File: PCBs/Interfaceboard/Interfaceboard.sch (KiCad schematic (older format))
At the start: 0 parts

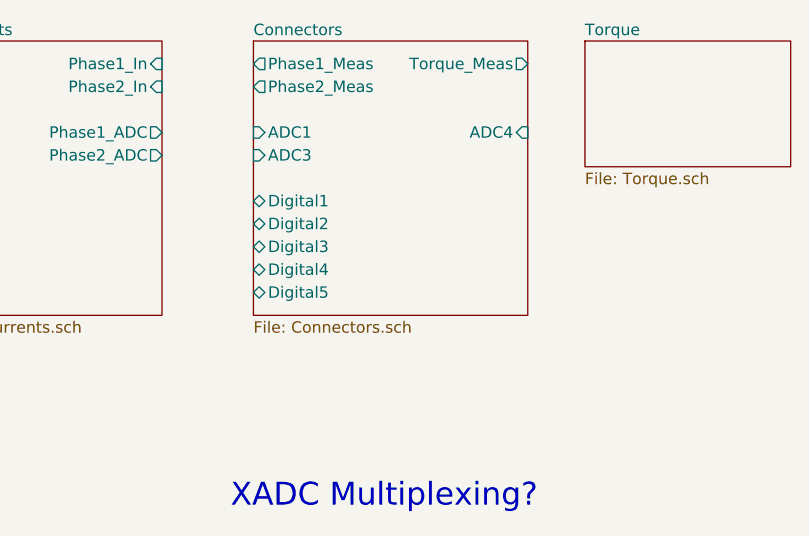
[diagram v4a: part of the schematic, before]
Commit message: Finished schematics for analog interface board. Ready for review and then PCB design.
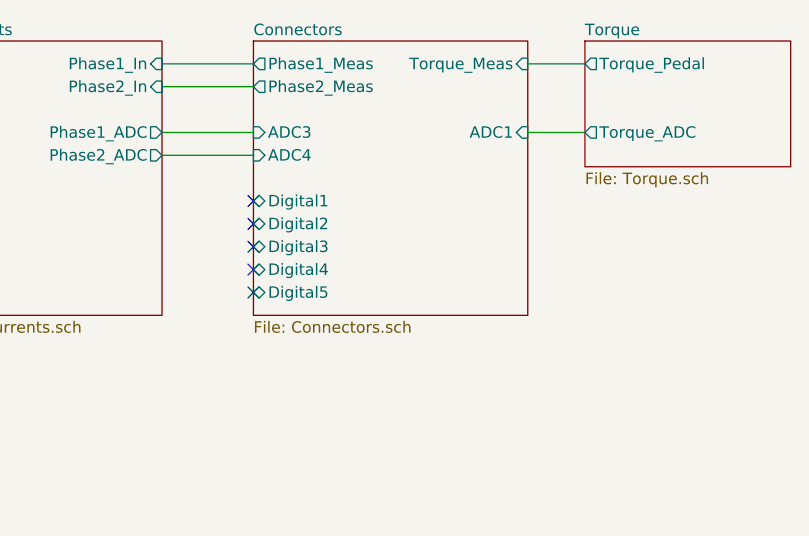
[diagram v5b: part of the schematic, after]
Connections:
- no-connect marks 0 -> 5
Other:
- note removed: "XADC Multiplexing?"
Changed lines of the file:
@@
 $EndDescr
-$Sheet
-S 4900 2400 1200 1200
-U 6040B42D
-F0 "Connectors" 50
-F1 "Connectors.sch" 50
-F2 "Phase1_Meas" O L 4900 2500 50
-F3 "Phase2_Meas" O L 4900 2600 50
-F4 "Torque_Meas" O R 6100 2500 50
-F5 "ADC1" I L 4900 2800 50
-F6 "ADC3" I L 4900 2900 50
-F7 "ADC4" I R 6100 2800 50
-F8 "Digital1" B L 4900 3100 50
-F9 "Digital2" B L 4900 3200 50
-F10 "Digital3" B L 4900 3300 50
-F11 "Digital4" B L 4900 3400 50
-F12 "Digital5" B L 4900 3500 50
-$EndSheet
 $Sheet
 S 3550 2400 950  1200
@@
 F0 "Torque" 50
 F1 "Torque.sch" 50
+F2 "Torque_Pedal" O L 6350 2500 50
+F3 "Torque_ADC" O L 6350 2800 50
 $EndSheet
-Text Notes 4800 4450 0    100  ~ 0
-XADC Multiplexing?
+Wire Wire Line
+	6350 2500 6100 2500
+Wire Wire Line
+	6100 2800 6350 2800
+Wire Wire Line
+	4500 2500 4900 2500
+Wire Wire Line
+	4900 2600 4500 2600
+Wire Wire Line
+	4500 2800 4900 2800
+Wire Wire Line
+	4900 2900 4500 2900
+$Sheet
+S 4900 2400 1200 1200
+U 6040B42D
+F0 "Connectors" 50
+F1 "Connectors.sch" 50
+F2 "Phase1_Meas" O L 4900 2500 50
+F3 "Phase2_Meas" O L 4900 2600 50
+F4 "Torque_Meas" I R 6100 2500 50
+F5 "ADC3" I L 4900 2800 50
+F6 "ADC4" I L 4900 2900 50
+F7 "ADC1" I R 6100 2800 50
+F8 "Digital1" B L 4900 3100 50
+F9 "Digital2" B L 4900 3200 50
+F10 "Digital3" B L 4900 3300 50
+F11 "Digital4" B L 4900 3400 50
+F12 "Digital5" B L 4900 3500 50
+$EndSheet
+NoConn ~ 4900 3100
+NoConn ~ 4900 3200
+NoConn ~ 4900 3300
+NoConn ~ 4900 3400
+NoConn ~ 4900 3500
 $EndSCHEMATC

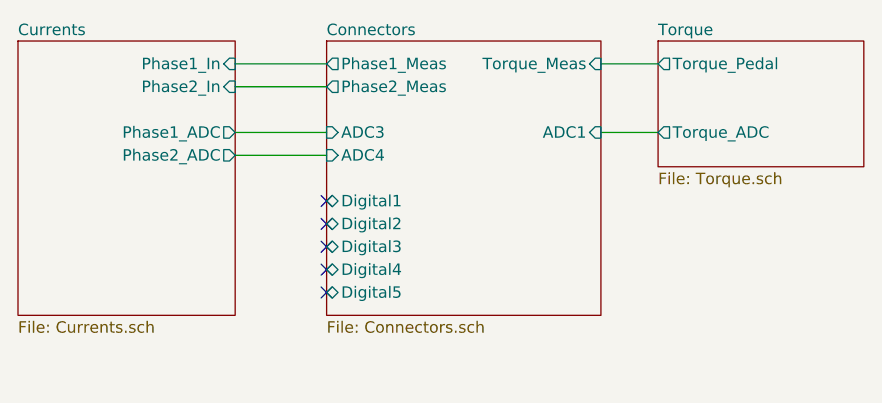
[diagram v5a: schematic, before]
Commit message: Added test points and final associated footprints. Made outline for PCB.
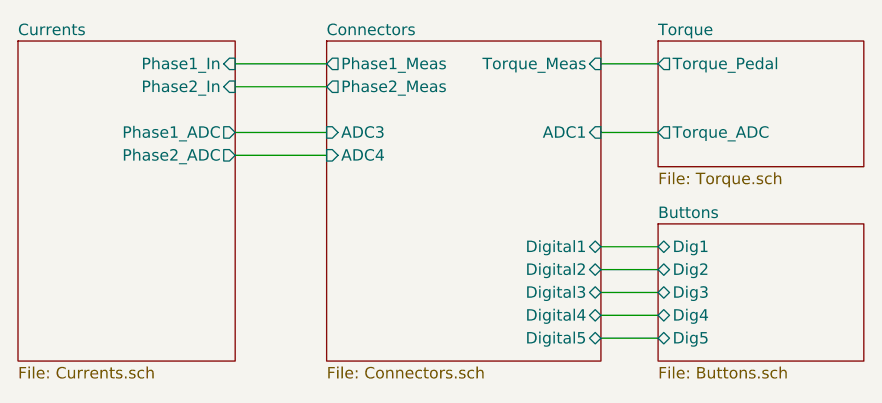
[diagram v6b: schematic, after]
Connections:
- no-connect marks 5 -> 0
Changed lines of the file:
@@
 $Descr A4 11693 8268
 encoding utf-8
-Sheet 1 4
-Title "Interface Board for Control of PMAC Motor in Electric Go-Kart"
-Date "2021-03-04"
+Sheet 1 5
+Title "Analog Board for Control of PMAC Motor in Electric Go-Kart"
+Date "2021-03-13"
 Rev "Version 1"
 Comp "University of Southern Denmark"
@@
 $EndDescr
 $Sheet
-S 3550 2400 950  1200
+S 3550 2400 950  1400
 U 6040B450
 F0 "Currents" 50
@@
 	4900 2900 4500 2900
 $Sheet
-S 4900 2400 1200 1200
+S 4900 2400 1200 1400
 U 6040B42D
 F0 "Connectors" 50
@@
 F6 "ADC4" I L 4900 2900 50
 F7 "ADC1" I R 6100 2800 50
-F8 "Digital1" B L 4900 3100 50
-F9 "Digital2" B L 4900 3200 50
-F10 "Digital3" B L 4900 3300 50
-F11 "Digital4" B L 4900 3400 50
-F12 "Digital5" B L 4900 3500 50
+F8 "Digital1" B R 6100 3300 50
+F9 "Digital2" B R 6100 3400 50
+F10 "Digital3" B R 6100 3500 50
+F11 "Digital4" B R 6100 3600 50
+F12 "Digital5" B R 6100 3700 50
 $EndSheet
-NoConn ~ 4900 3100
-NoConn ~ 4900 3200
-NoConn ~ 4900 3300
-NoConn ~ 4900 3400
-NoConn ~ 4900 3500
+$Sheet
+S 6350 3200 900  600
+U 604F3ED7
+F0 "Buttons" 50
+F1 "Buttons.sch" 50
+F2 "Dig1" B L 6350 3300 50
+F3 "Dig2" B L 6350 3400 50
+F4 "Dig3" B L 6350 3500 50
+F5 "Dig4" B L 6350 3600 50
+F6 "Dig5" B L 6350 3700 50
+$EndSheet
+Wire Wire Line
+	6350 3300 6100 3300
+Wire Wire Line
+	6100 3400 6350 3400
+Wire Wire Line
+	6350 3500 6100 3500
+Wire Wire Line
+	6100 3600 6350 3600
+Wire Wire Line
+	6350 3700 6100 3700
 $EndSCHEMATC

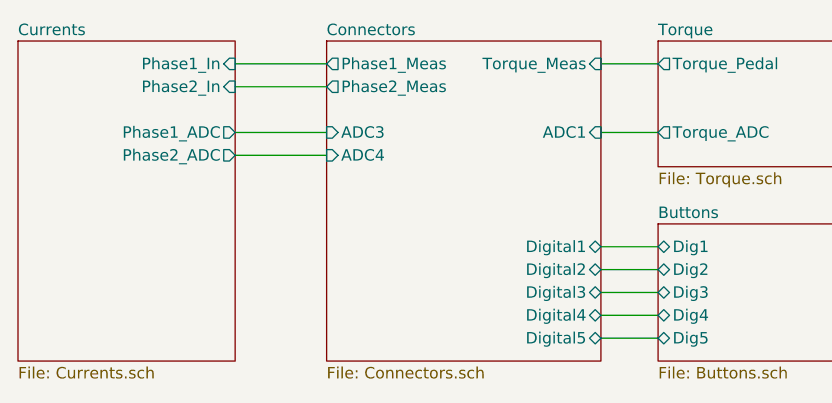
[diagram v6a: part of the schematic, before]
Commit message: Removed some buttons and added LEDs. Finished placing the components on the PCB.
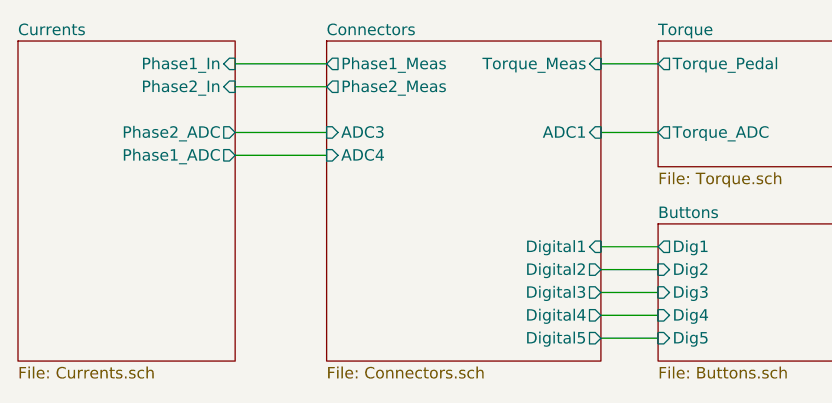
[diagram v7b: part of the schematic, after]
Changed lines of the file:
@@
 F2 "Phase1_In" I R 4500 2500 50
 F3 "Phase2_In" I R 4500 2600 50
-F4 "Phase1_ADC" O R 4500 2800 50
-F5 "Phase2_ADC" O R 4500 2900 50
+F4 "Phase1_ADC" O R 4500 2900 50
+F5 "Phase2_ADC" O R 4500 2800 50
 $EndSheet
 $Sheet
@@
 F6 "ADC4" I L 4900 2900 50
 F7 "ADC1" I R 6100 2800 50
-F8 "Digital1" B R 6100 3300 50
-F9 "Digital2" B R 6100 3400 50
-F10 "Digital3" B R 6100 3500 50
-F11 "Digital4" B R 6100 3600 50
-F12 "Digital5" B R 6100 3700 50
+F8 "Digital1" I R 6100 3300 50
+F9 "Digital2" O R 6100 3400 50
+F10 "Digital3" O R 6100 3500 50
+F11 "Digital4" O R 6100 3600 50
+F12 "Digital5" O R 6100 3700 50
 $EndSheet
 $Sheet
@@
 F0 "Buttons" 50
 F1 "Buttons.sch" 50
-F2 "Dig1" B L 6350 3300 50
-F3 "Dig2" B L 6350 3400 50
-F4 "Dig3" B L 6350 3500 50
-F5 "Dig4" B L 6350 3600 50
-F6 "Dig5" B L 6350 3700 50
+F2 "Dig1" O L 6350 3300 50
+F3 "Dig2" I L 6350 3400 50
+F4 "Dig3" I L 6350 3500 50
+F5 "Dig4" I L 6350 3600 50
+F6 "Dig5" I L 6350 3700 50
 $EndSheet
 Wire Wire Line

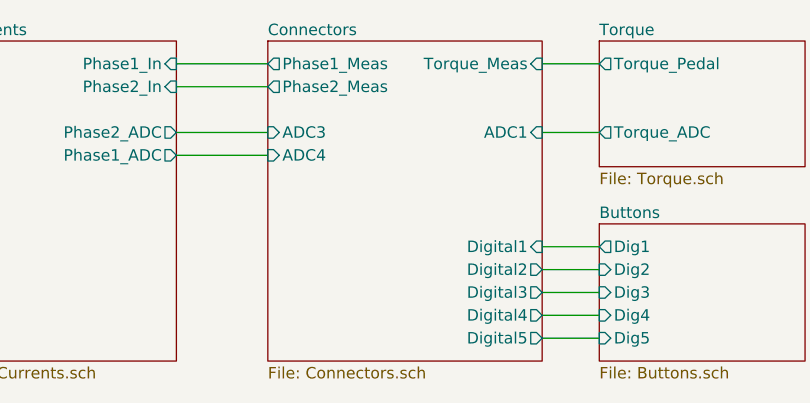
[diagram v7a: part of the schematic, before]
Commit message: Swapped some ADC channels for the signals to ensure that simultaneous conversion is possible.
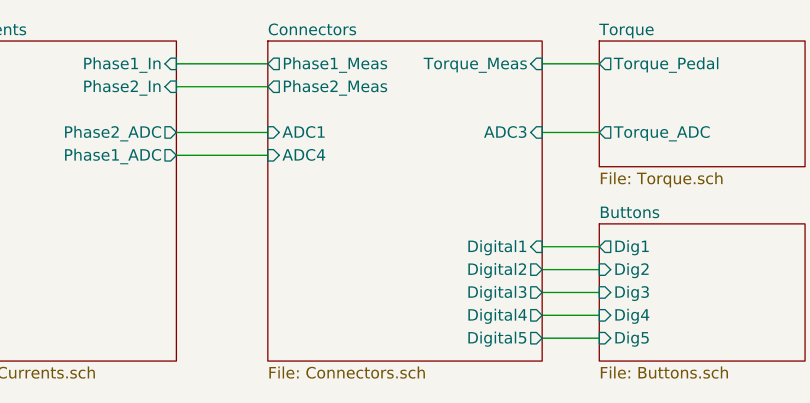
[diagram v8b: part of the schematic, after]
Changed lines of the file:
@@
 F3 "Phase2_Meas" O L 4900 2600 50
 F4 "Torque_Meas" I R 6100 2500 50
-F5 "ADC3" I L 4900 2800 50
+F5 "ADC1" I L 4900 2800 50
 F6 "ADC4" I L 4900 2900 50
-F7 "ADC1" I R 6100 2800 50
+F7 "ADC3" I R 6100 2800 50
 F8 "Digital1" I R 6100 3300 50
 F9 "Digital2" O R 6100 3400 50
